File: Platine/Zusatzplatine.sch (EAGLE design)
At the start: 16 parts

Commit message: - Platine erweitert
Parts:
- added JP2: (no value), pinhead:PINHD-2X19
- added WLAN_/RESET, WLAN_3.3V, WLAN_GND, WLAN_GPIO0, WLAN_GPIO1, WLAN_PD, WLAN_RX, WLAN_TX: SE14, solpad:SE14
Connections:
- net N$1 renamed +3.3V
- new net N$1: JP2.29, WLAN_/RESET.MP
- new net N$11: JP2.31, WLAN_GPIO1.MP
- new net N$12: JP2.33, WLAN_PD.MP
- new net N$13: JP2.35, WLAN_RX.MP
- new net N$14: JP2.37, WLAN_TX.MP
- new net N$15: JP2.34, WLAN_GPIO0.MP
- new net N$16: JP2.20, WLAN_GND.MP
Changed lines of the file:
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@@
 <?xml version="1.0" encoding="utf-8"?>
 <!DOCTYPE eagle SYSTEM "eagle.dtd">
-<eagle version="7.2.0">
+<eagle version="7.3.0">
 <drawing>
 <settings>
@@
 <part name="D2" library="diode" deviceset="1N4148" device="DO35-7"/>
 <part name="D3" library="diode" deviceset="P6KEXXA" device=""/>
+<part name="JP2" library="pinhead" deviceset="PINHD-2X19" device=""/>
+<part name="WLAN_3.3V" library="solpad" deviceset="SE14" device=""/>
+<part name="WLAN_GND" library="solpad" deviceset="SE14" device=""/>
+<part name="WLAN_TX" library="solpad" deviceset="SE14" device=""/>
+<part name="WLAN_RX" library="solpad" deviceset="SE14" device=""/>
+<part name="WLAN_PD" library="solpad" deviceset="SE14" device=""/>
+<part name="WLAN_GPIO0" library="solpad" deviceset="SE14" device=""/>
+<part name="WLAN_GPIO1" library="solpad" deviceset="SE14" device=""/>
+<part name="WLAN_/RESET" library="solpad" deviceset="SE14" device=""/>
 </parts>
 <sheets>
@@
 <instance part="D2" gate="G$1" x="109.22" y="55.88" rot="R90"/>
 <instance part="D3" gate="1" x="96.52" y="55.88" rot="R90"/>
+<instance part="JP2" gate="G$1" x="170.18" y="58.42"/>
+<instance part="WLAN_3.3V" gate="1" x="152.4" y="88.9"/>
+<instance part="WLAN_GND" gate="1" x="187.96" y="55.88" rot="R270"/>
+<instance part="WLAN_TX" gate="1" x="147.32" y="33.02" rot="R90"/>
+<instance part="WLAN_RX" gate="1" x="149.86" y="35.56" rot="R90"/>
+<instance part="WLAN_PD" gate="1" x="152.4" y="38.1" rot="R90"/>
+<instance part="WLAN_GPIO0" gate="1" x="187.96" y="38.1" rot="R270"/>
+<instance part="WLAN_GPIO1" gate="1" x="154.94" y="40.64" rot="R90"/>
+<instance part="WLAN_/RESET" gate="1" x="157.48" y="43.18" rot="R90"/>
 </instances>
 <busses>
@@
 </segment>
 </net>
-<net name="N$1" class="0">
+<net name="+3.3V" class="0">
 <segment>
 <pinref part="JP1" gate="G$1" pin="5"/>
 <pinref part="IR_VDD" gate="1" pin="MP"/>
 <wire x1="38.1" y1="71.12" x2="17.78" y2="71.12" width="0.1524" layer="91"/>
+<label x="20.32" y="71.12" size="1.778" layer="95"/>
+</segment>
+<segment>
+<wire x1="152.4" y1="86.36" x2="132.08" y2="86.36" width="0.1524" layer="91"/>
+<label x="139.7" y="86.36" size="1.778" layer="95"/>
 </segment>
 </net>
@@
 </segment>
 </net>
+<net name="N$1" class="0">
+<segment>
+<pinref part="WLAN_/RESET" gate="1" pin="MP"/>
+<pinref part="JP2" gate="G$1" pin="29"/>
+<wire x1="160.02" y1="43.18" x2="167.64" y2="43.18" width="0.1524" layer="91"/>
+</segment>
+</net>
+<net name="N$11" class="0">
+<segment>
+<pinref part="JP2" gate="G$1" pin="31"/>
+<pinref part="WLAN_GPIO1" gate="1" pin="MP"/>
+<wire x1="167.64" y1="40.64" x2="157.48" y2="40.64" width="0.1524" layer="91"/>
+</segment>
+</net>
+<net name="N$12" class="0">
+<segment>
+<pinref part="WLAN_PD" gate="1" pin="MP"/>
+<pinref part="JP2" gate="G$1" pin="33"/>
+<wire x1="154.94" y1="38.1" x2="167.64" y2="38.1" width="0.1524" layer="91"/>
+</segment>
+</net>
+<net name="N$13" class="0">
+<segment>
+<pinref part="JP2" gate="G$1" pin="35"/>
+<pinref part="WLAN_RX" gate="1" pin="MP"/>
+<wire x1="167.64" y1="35.56" x2="152.4" y2="35.56" width="0.1524" layer="91"/>
+</segment>
+</net>
+<net name="N$14" class="0">
+<segment>
+<pinref part="WLAN_TX" gate="1" pin="MP"/>
+<pinref part="JP2" gate="G$1" pin="37"/>
+<wire x1="149.86" y1="33.02" x2="167.64" y2="33.02" width="0.1524" layer="91"/>
+</segment>
+</net>
+<net name="N$15" class="0">
+<segment>
+<pinref part="JP2" gate="G$1" pin="34"/>
+<pinref part="WLAN_GPIO0" gate="1" pin="MP"/>
+<wire x1="175.26" y1="38.1" x2="185.42" y2="38.1" width="0.1524" layer="91"/>
+</segment>
+</net>
+<net name="N$16" class="0">
+<segment>
+<pinref part="WLAN_GND" gate="1" pin="MP"/>
+<pinref part="JP2" gate="G$1" pin="20"/>
+<wire x1="185.42" y1="55.88" x2="175.26" y2="55.88" width="0.1524" layer="91"/>
+</segment>
+</net>

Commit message: - Platine weiter
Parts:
- removed D3: P6KEXXA, diode:P6KEXXA
- added D4: SM6T6V8A, diode:SUPPRESSOR-SMBG
- added DCF_3.3V, DCF_DATA, DCF_GND, DCF_POWON: SE14, solpad:SE14
- D1, D2: value 1N4148DO35-7 -> 1N4148WS; device diode:1N4148DO35-7 -> Diodes:1N4148WS
- R1, R2: device rcl:R-EU_0309/12 -> rcl:R-EU_R1206
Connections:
- removed net N$9: D2.A, D3.A
- new net N$17: DCF_GND.MP, JP2.9
- new net N$18: DCF_3.3V.MP, JP2.7
- new net N$19: DCF_POWON.MP, JP2.1
- new net N$20: DCF_DATA.MP, JP2.2
- net +3.3V: now also WLAN_3.3V.MP
- net N$10: now also D1.1, D4.C; no longer D1.C, D3.C
- net N$4: now also D2.0, D4.A
- net N$7: no longer D1.A, D2.C
- net N$8: now also D1.0, D2.1
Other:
- moved on the sheet: D1, D2, R1, WLAN_3.3V

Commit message: - Platine Fehler behoben
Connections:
- removed net N$5: 5V_IN.MP, JP1.6, R2.2, WS_5V.MP
- net N$10: now also 5V_IN.MP, JP1.6, R2.2, WS_5V.MP

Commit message: - Platine überarbeitet
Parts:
- removed 5V_GND, 5V_IN: SE14, solpad:SE14
- added SUP_+5V, SUP_GND: SE14, solpad:SE14
- D4: device diode:SUPPRESSOR-SMBG -> diode:SUPPRESSOR-SMBJ
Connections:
- net N$7 renamed LED-OUT
- removed net N$10: 5V_IN.MP, D1.1, D4.C, JP1.6, R2.2, WS_5V.MP
- removed net N$16: JP2.20, WLAN_GND.MP
- removed net N$17: DCF_GND.MP, JP2.9
- new net +5V: D1.1, D4.C, JP1.6, R2.2, SUP_+5V.MP, WS_5V.MP
- new net GND: D2.0, D4.A, DCF_GND.MP, IR_GND.MP, JP1.20, JP1.22, JP1.8, JP2.20, JP2.9, SUP_GND.MP, WLAN_GND.MP, WS_GND.MP
- net N$4: now also JP1.19; no longer 5V_GND.MP, D2.0, D4.A, IR_GND.MP, JP1.8, WS_GND.MP
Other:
- moved on the sheet: IR_GND, IR_IN, IR_VDD, LDR_GND, LDR_IN, R2, WS_5V, WS_DIGOUT, WS_GND

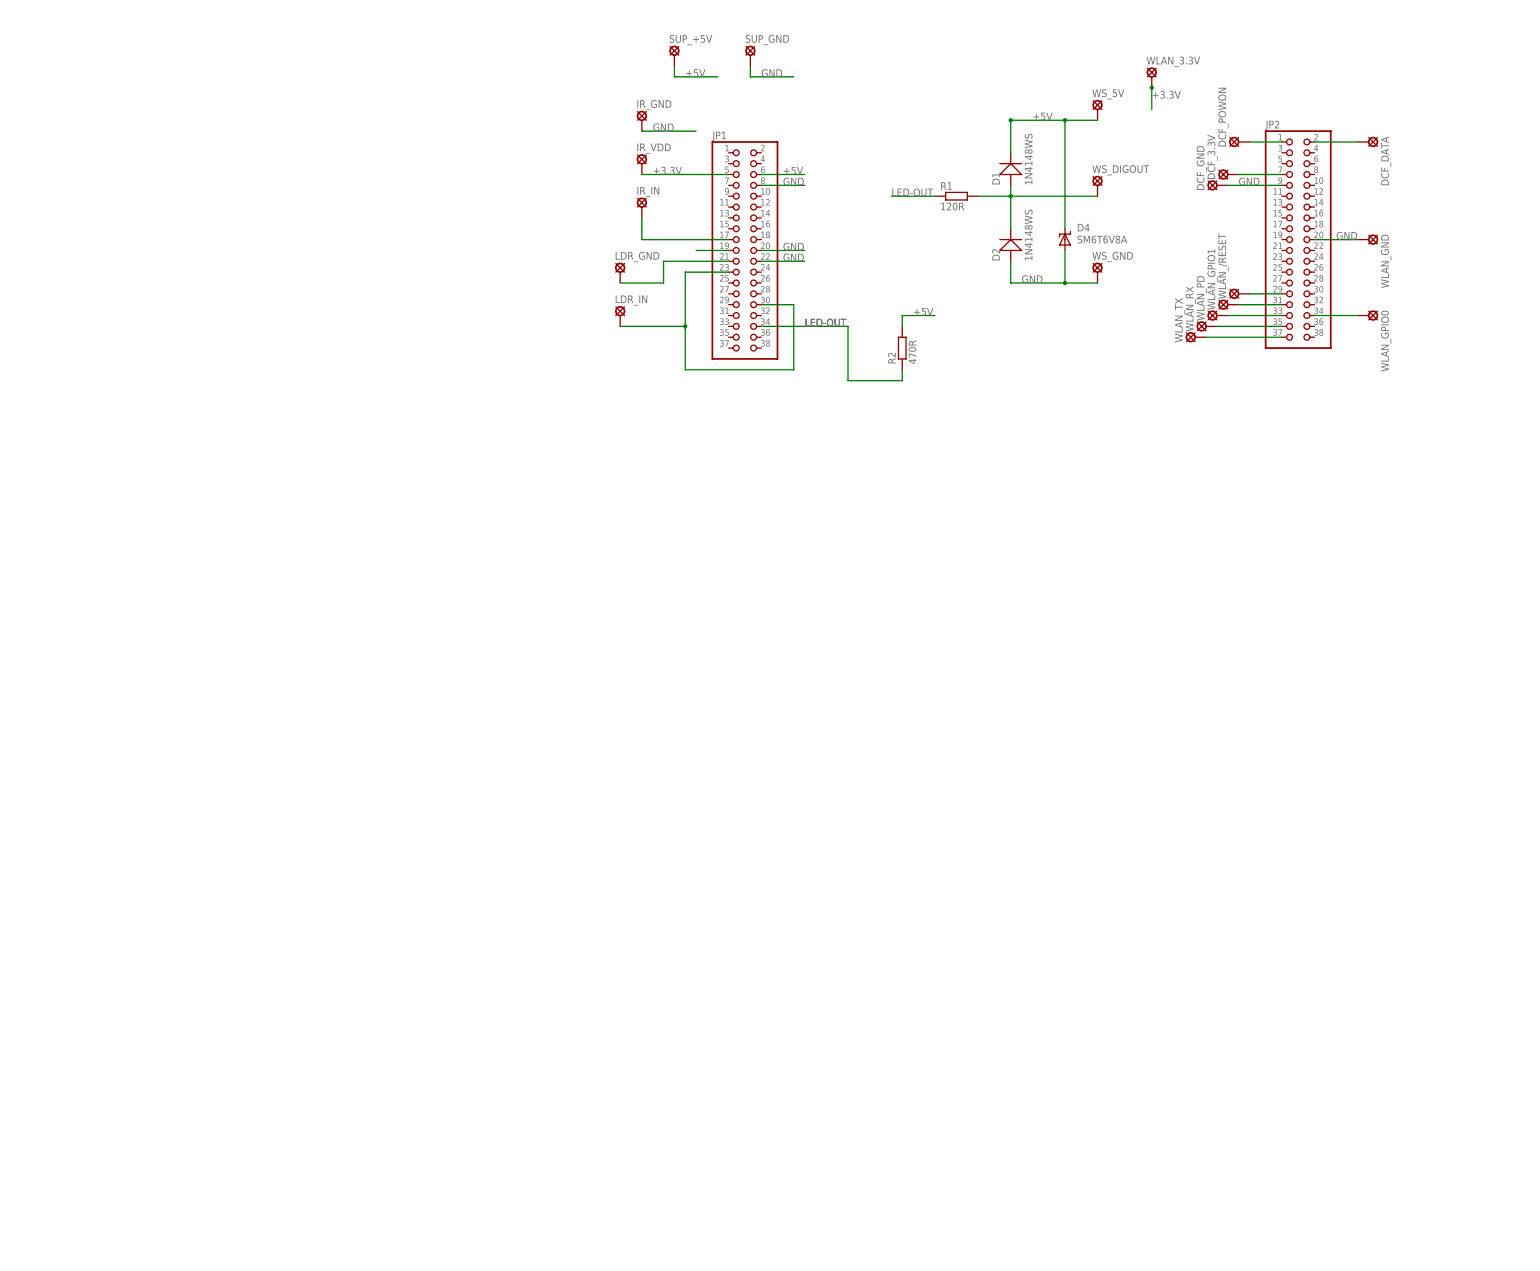
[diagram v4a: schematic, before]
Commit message: - Platine auf Arduino Connectors umgestellt
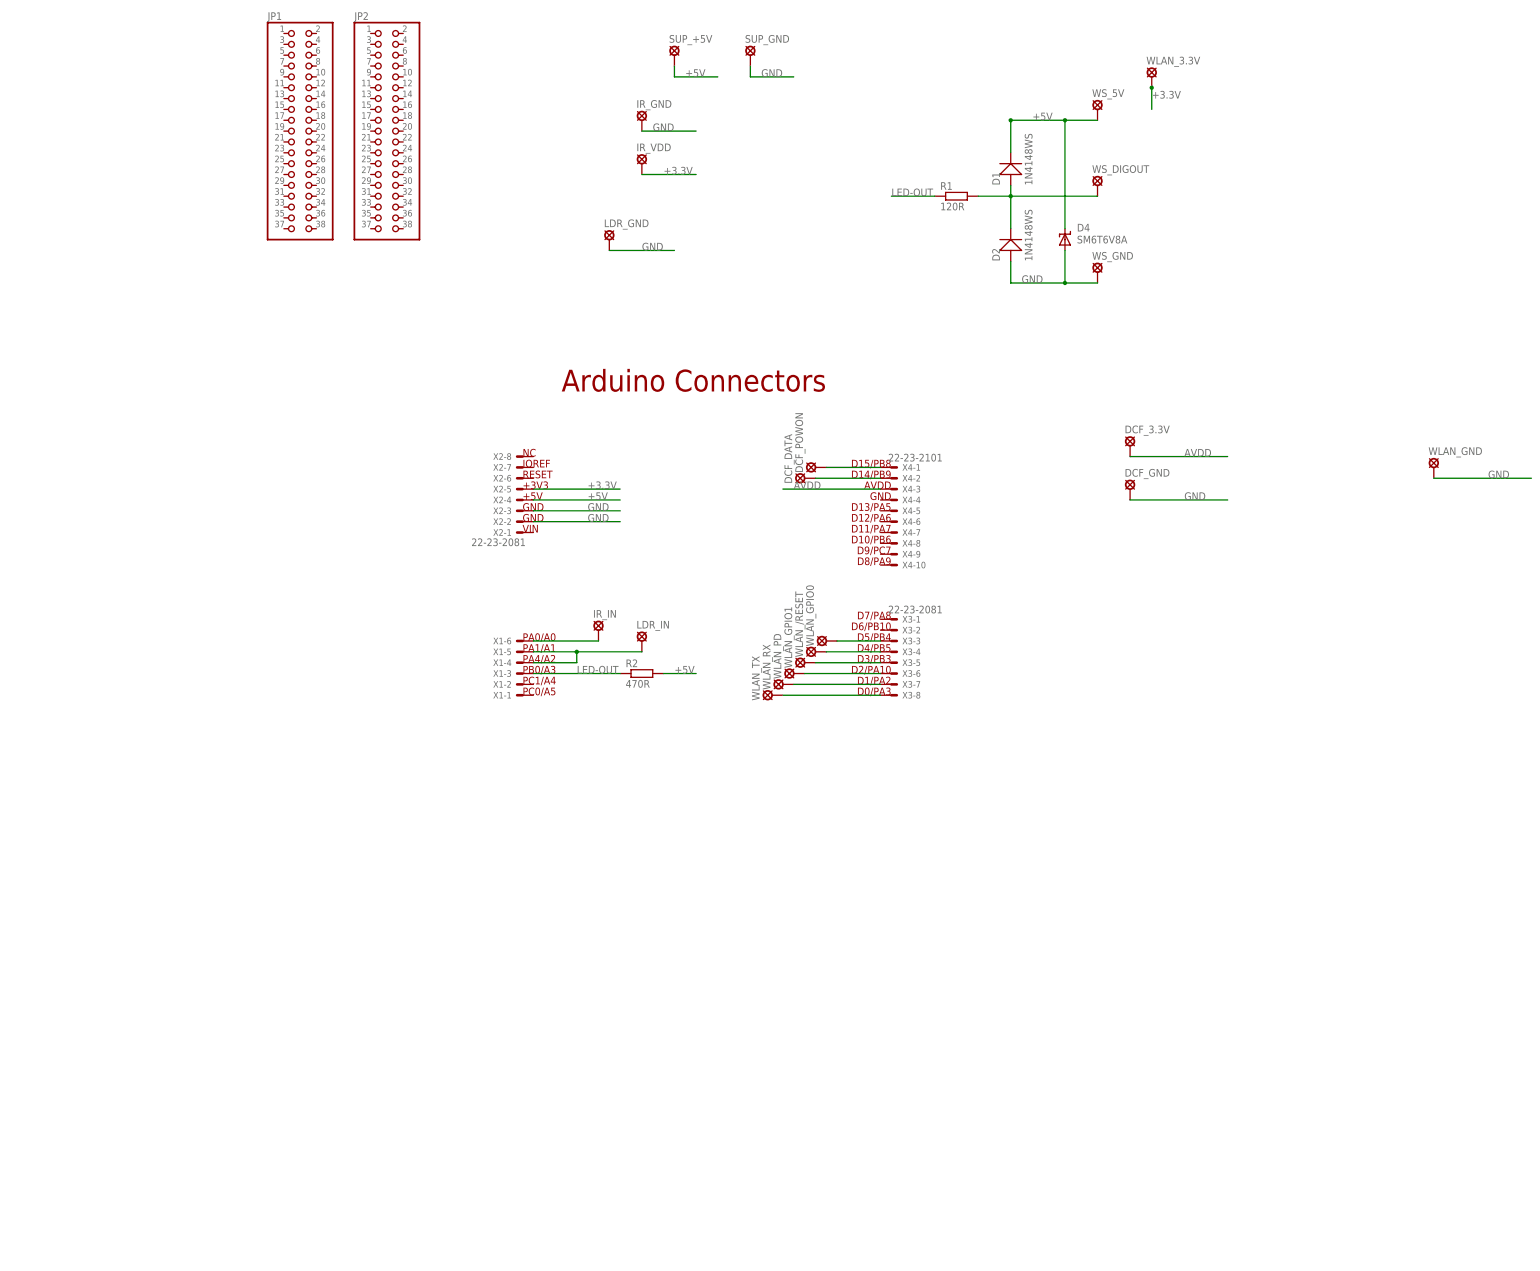
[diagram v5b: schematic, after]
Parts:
- added X1: (no value), con-molex:22-23-2061
- added X2, X3: 22-23-2081, con-molex:22-23-2081
- added X4: 22-23-2101, con-molex:22-23-2101
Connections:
- removed net N$12: JP2.33, WLAN_PD.MP
- removed net N$13: JP2.35, WLAN_RX.MP
- removed net N$14: JP2.37, WLAN_TX.MP
- removed net N$15: JP2.34, WLAN_GPIO0.MP
- removed net N$18: DCF_3.3V.MP, JP2.7
- removed net N$19: DCF_POWON.MP, JP2.1
- removed net N$20: DCF_DATA.MP, JP2.2
- new net AVDD: X4-3.S
- new net N$10: DCF_POWON.MP, X4-1.S
- new net N$5: WLAN_PD.MP, X3-6.S
- new net N$7: WLAN_/RESET.MP, X3-4.S
- new net N$9: WLAN_GPIO0.MP, X3-3.S
- net +3.3V: now also X2-5.S; no longer JP1.5
- net +5V: now also X2-4.S; no longer JP1.6
- net GND: now also LDR_GND.MP, X2-2.S, X2-3.S; no longer JP1.20, JP1.22, JP1.8, JP2.20, JP2.9, WLAN_GND.MP
- net LED-OUT: now also X1-3.S; no longer JP1.34
- net N$1: now also WLAN_TX.MP, X3-8.S; no longer JP2.29, WLAN_/RESET.MP
- net N$11: now also DCF_DATA.MP, X4-2.S; no longer JP2.31, WLAN_GPIO1.MP
- net N$2: now also X1-6.S; no longer JP1.17
- net N$3: now also LDR_IN.MP, X1-4.S, X1-5.S; no longer JP1.21, LDR_GND.MP
- net N$4: now also WLAN_RX.MP, X3-7.S; no longer JP1.19
- net N$6: now also WLAN_GPIO1.MP, X3-5.S; no longer JP1.23, JP1.30, LDR_IN.MP
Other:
- note added: "+3V3"
- note added: "+5V"
- note added: "AVDD"
- note added: "Arduino Connectors"
- note added: "D0/PA3"
- note added: "D1/PA2"
- note added: "D10/PB6"
- note added: "D11/PA7"
- note added: "D12/PA6"
- note added: "D13/PA5"
- note added: "D14/PB9"
- note added: "D15/PB8"
- note added: "D2/PA10"
- note added: "D3/PB3"
- note added: "D4/PB5"
- note added: "D5/PB4"
- note added: "D6/PB10"
- note added: "D7/PA8"
- note added: "D8/PA9"
- note added: "D9/PC7"
- note added: "GND"
- note added: "IOREF"
- note added: "NC"
- note added: "PA0/A0"
- note added: "PA1/A1"
- note added: "PA4/A2"
- note added: "PB0/A3"
- note added: "PC0/A5"
- note added: "PC1/A4"
- note added: "RESET"
- note added: "VIN"
- moved on the sheet: DCF_3.3V, DCF_DATA, DCF_GND, DCF_POWON, IR_IN, JP1, JP2, LDR_GND, LDR_IN, R2, WLAN_/RESET, WLAN_GND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

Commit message: - Platine überarbeitet
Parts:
- removed JP1, JP2: (no value), pinhead:PINHD-2X19
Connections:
- net AVDD: now also DCF_3.3V.MP
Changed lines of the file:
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@@
 </classes>
 <parts>
-<part name="JP1" library="pinhead" deviceset="PINHD-2X19" device=""/>
 <part name="SUP_+5V" library="solpad" deviceset="SE14" device=""/>
 <part name="SUP_GND" library="solpad" deviceset="SE14" device=""/>
@@
 <part name="R2" library="rcl" deviceset="R-EU_" device="R1206" value="470R"/>
 <part name="WS_DIGOUT" library="solpad" deviceset="SE14" device=""/>
-<part name="JP2" library="pinhead" deviceset="PINHD-2X19" device=""/>
 <part name="WLAN_3.3V" library="solpad" deviceset="SE14" device=""/>
 <part name="WLAN_GND" library="solpad" deviceset="SE14" device=""/>
@@
 </plain>
 <instances>
-<instance part="JP1" gate="G$1" x="-63.5" y="83.82"/>
 <instance part="SUP_+5V" gate="1" x="25.4" y="99.06"/>
 <instance part="SUP_GND" gate="1" x="43.18" y="99.06"/>
@@
 <instance part="R2" gate="G$1" x="17.78" y="-45.72"/>
 <instance part="WS_DIGOUT" gate="1" x="124.46" y="68.58"/>
-<instance part="JP2" gate="G$1" x="-43.18" y="83.82"/>
 <instance part="WLAN_3.3V" gate="1" x="137.16" y="93.98"/>
 <instance part="WLAN_GND" gate="1" x="203.2" y="2.54"/>
@@
 <wire x1="154.94" y1="5.08" x2="132.08" y2="5.08" width="0.1524" layer="91"/>
 <label x="144.78" y="5.08" size="1.778" layer="95"/>
-</segment>
-</net>
+<pinref part="DCF_3.3V" gate="1" pin="MP"/>
+</segment>
+</net>

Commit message: Reworked Board Design
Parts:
- removed DCF_3.3V, DCF_DATA, DCF_GND, DCF_POWON, SUP_+5V, SUP_GND, WLAN_/RESET, WLAN_3.3V, WLAN_GND, WLAN_GPIO0, WLAN_GPIO1, WLAN_PD, WLAN_RX, WLAN_TX: SE14, solpad:SE14
- removed X1: (no value), con-molex:22-23-2061
- removed X2, X3: 22-23-2081, con-molex:22-23-2081
- removed X4: 22-23-2101, con-molex:22-23-2101
- added DBG_CON: (no value), con-lstb:MA05-1
- added DCF1: (no value), con-lstb:MA04-1
- added HOLE_EXT_+5V, HOLE_EXT_GND: WIREPAD3,17/1,3, wirepad:WIREPAD3,17/1,3
- added PAD_EXT_+5V, PAD_EXT_+5V1, PAD_EXT_GND, PAD_EXT_GND1: WIREPADSMD2,54-5,08, wirepad:WIREPADSMD2,54-5,08
- added U$1: NUCLEO_F411RE, Stm32nucleo:NUCLEO_F411RE
- added U$2: ESP01, esp8266modules:ESP01
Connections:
- removed net +3.3V: IR_VDD.MP, WLAN_3.3V.MP, X2-5.S
- removed net AVDD: DCF_3.3V.MP, X4-3.S
- removed net N$10: DCF_POWON.MP, X4-1.S
- removed net N$11: DCF_DATA.MP, X4-2.S
- removed net N$3: LDR_IN.MP, X1-4.S, X1-5.S
- removed net N$4: WLAN_RX.MP, X3-7.S
- removed net N$5: WLAN_PD.MP, X3-6.S
- removed net N$6: WLAN_GPIO1.MP, X3-5.S
- removed net N$7: WLAN_/RESET.MP, X3-4.S
- removed net N$9: WLAN_GPIO0.MP, X3-3.S
- new net +3V3: IR_VDD.MP, U$1.3V, U$1.3V3, U$2.VCC
- new net DCF1_DATA: DCF1.3, U$1.PB9
- new net DCF1_PON: DCF1.4, U$1.PB8
- new net IR_IN: IR_IN.MP, U$1.A0
- new net LDR_IN: LDR_IN.MP, U$1.A1, U$1.A2
- new net N$12: U$1.D5, U$2.GPIO0
- new net N$13: U$1.D4, U$2.RST
- new net N$14: U$1.D3, U$2.CH_PD
- new net N$15: U$1.D0, U$2.TXD
- new net N$16: U$1.D1, U$2.RXD
- new net N$17: U$1.D2, U$2.GPIO2
- new net NRST: DBG_CON.4, U$1.NRESET
- new net SWCLK: DBG_CON.1, U$1.PA14
- new net SWDIO: DBG_CON.3, U$1.PA13
- new net SWO: DBG_CON.5
- net +5V: now also HOLE_EXT_+5V.P, PAD_EXT_+5V.P, PAD_EXT_+5V1.P, R2.1, U$1.E5V; no longer R2.2, SUP_+5V.MP, X2-4.S
- net GND: now also DBG_CON.2, DCF1.2, HOLE_EXT_GND.P, PAD_EXT_GND.P, PAD_EXT_GND1.P, U$1.AGND, U$1.GND8, U$2.GND; no longer DCF_GND.MP, SUP_GND.MP, X2-2.S, X2-3.S
- net LED-OUT: now also R2.2, U$1.A3; no longer R2.1, X1-3.S
- net N$1: now also DCF1.1, U$1.AREF; no longer WLAN_TX.MP, X3-8.S
- net N$2: now also U$1.5V, U$1.5V2; no longer IR_IN.MP, X1-6.S
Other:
- note added: "DCF"
- note added: "EXTERNAL SUPPLY"
- note added: "IR"
- note added: "LDR"
- note added: "SWD"
- note added: "WS PROTECTION"
- note removed: "+3V3"
- note removed: "+5V"
- note removed: "AVDD"
- note removed: "Arduino Connectors"
- note removed: "D0/PA3"
- note removed: "D1/PA2"
- note removed: "D10/PB6"
- note removed: "D11/PA7"
- note removed: "D12/PA6"
- note removed: "D13/PA5"
- note removed: "D14/PB9"
- note removed: "D15/PB8"
- note removed: "D2/PA10"
- note removed: "D3/PB3"
- note removed: "D4/PB5"
- note removed: "D5/PB4"
- note removed: "D6/PB10"
- note removed: "D7/PA8"
- note removed: "D8/PA9"
- note removed: "D9/PC7"
- note removed: "GND"
- note removed: "IOREF"
- note removed: "NC"
- note removed: "PA0/A0"
- note removed: "PA1/A1"
- note removed: "PA4/A2"
- note removed: "PB0/A3"
- note removed: "PC0/A5"
- note removed: "PC1/A4"
- note removed: "RESET"
- note removed: "VIN"
- moved on the sheet: D1, D2, D4, IR_GND, IR_IN, IR_VDD, LDR_GND, LDR_IN, R1, R2, WS_5V, WS_DIGOUT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
